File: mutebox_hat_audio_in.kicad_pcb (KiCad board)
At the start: 2 copper layers, 65 x 56 mm, 56 parts, among them J1 GPIO, J2 PLR237/T10BK, J3 RCJ-042, J4 RCJ-042, U2 74LVC157, U3 PCM1862DBT, U5 DIR9001PW, Y3 XO32

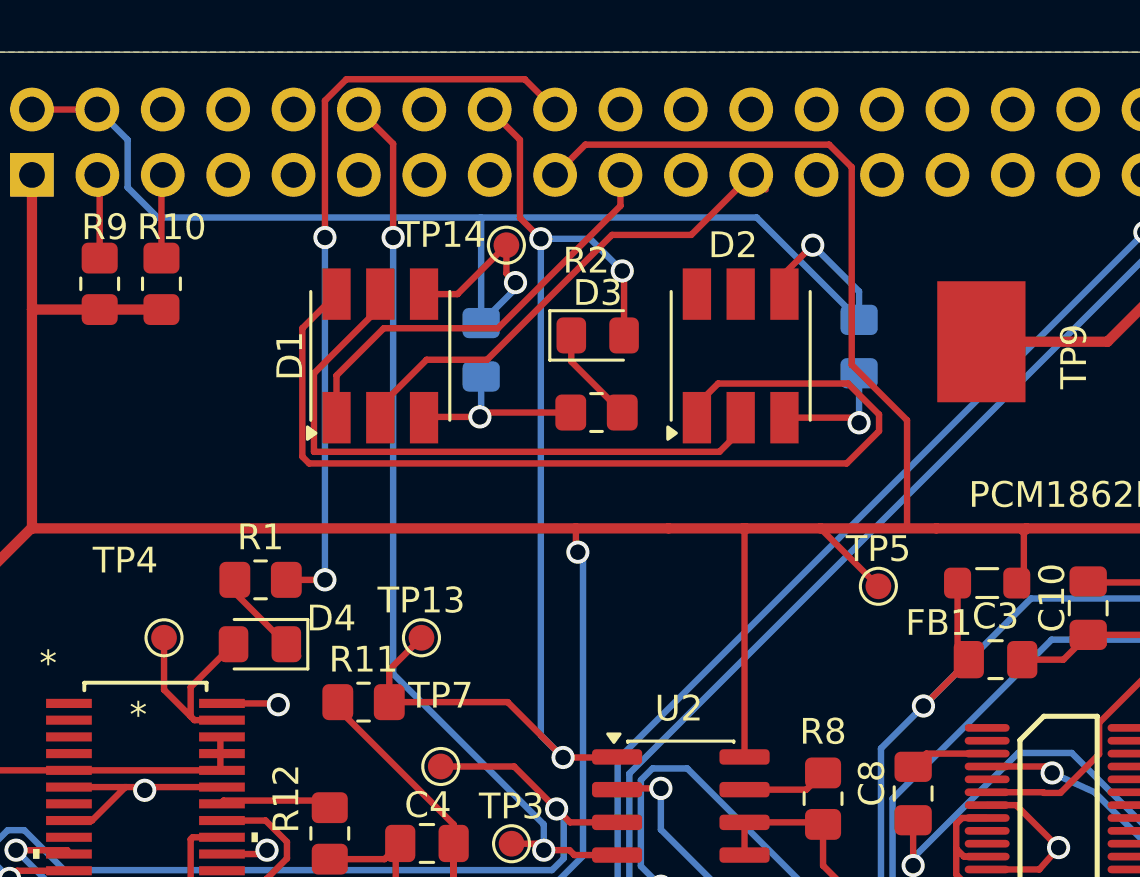
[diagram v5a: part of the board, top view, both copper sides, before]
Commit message: Moved dotstar caps to front of board.
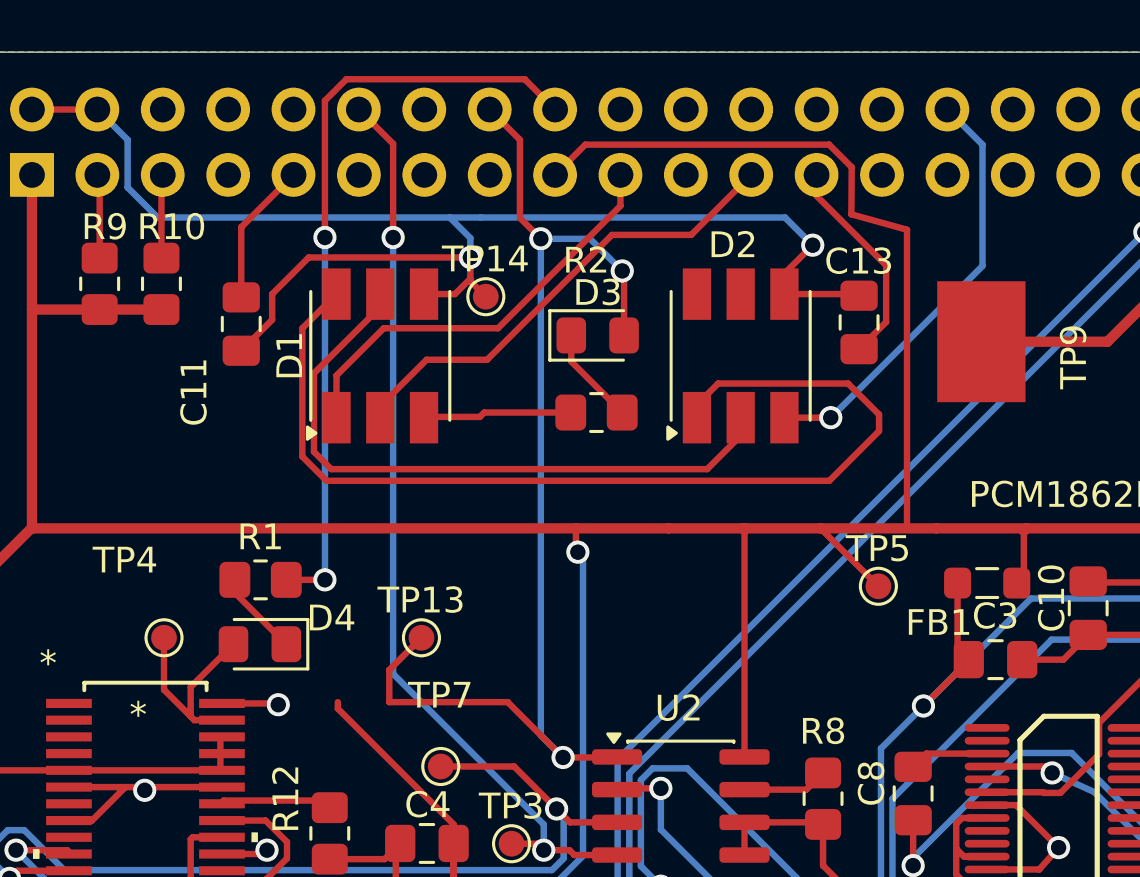
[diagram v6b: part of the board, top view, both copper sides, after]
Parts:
- removed R11: 100k, Resistor_SMD:R_0805_2012Metric_Pad1.20x1.40mm_HandSolder
- C11, C13: moved to F.Cu
- R8: value 100k -> 10k
- moved C11 9.37 mm to (116.5, 54.6), turned to 90 degrees
- moved TP14 2.15 mm to (126.0, 53.5)
- moved C13 0.94 mm to (140.5, 54.5)
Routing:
- net GND: track 155.8 -> 179.9 mm, vias 8 -> 7
- net Net-(D1-CO): track 24.6 -> 25.8 mm
- net /GPIO11/SPI0.SCLK: track 20.6 -> 19.8 mm
- net +3V3: track 178.8 -> 179.6 mm
- net Net-(D1-DO): track 39.0 -> 39.5 mm
